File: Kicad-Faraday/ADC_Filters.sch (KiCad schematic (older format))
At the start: 14 parts

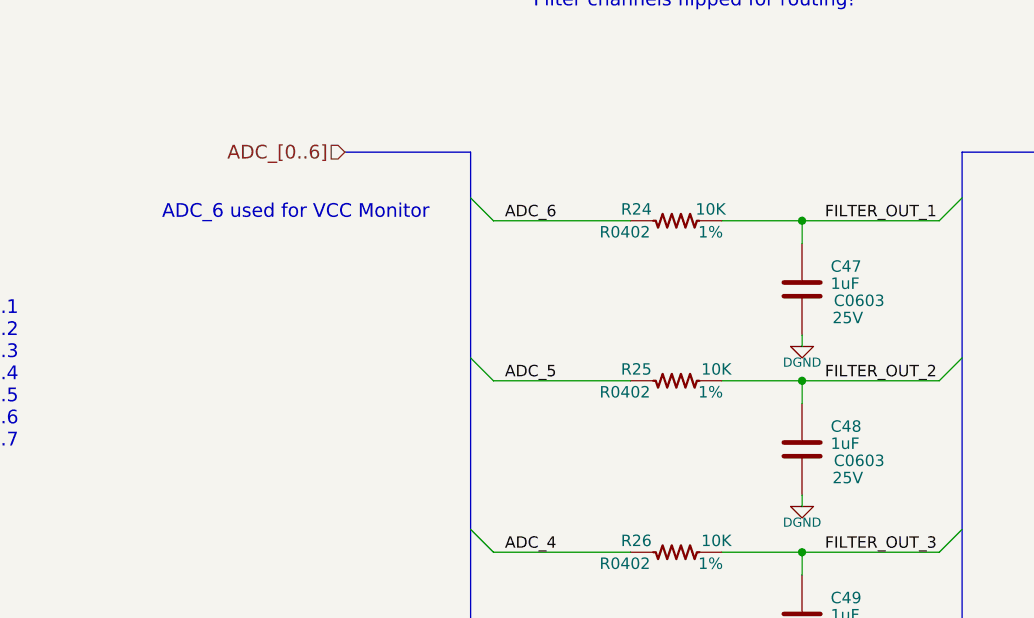
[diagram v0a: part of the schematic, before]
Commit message: Updated several items from the Rev B to C updates including microphone RC filter and CC1190 inductor footprints.
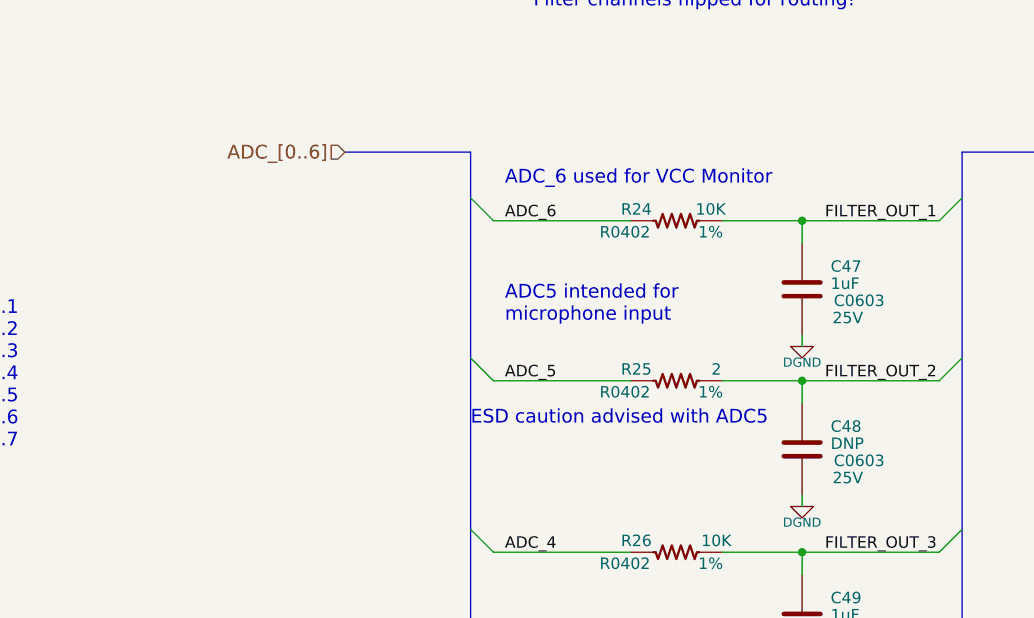
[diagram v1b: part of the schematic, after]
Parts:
- C48: value 1uF -> DNP
- R25: value 10K -> 2
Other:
- note added: "ADC5 intended for\nmicrophone input"
- note added: "ESD caution advised with ADC5"
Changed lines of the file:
@@
 Sheet 4 11
 Title "Faraday Wireless Node"
-Date "8 aug 2016"
+Date "18 oct 2016"
 Rev "C"
 Comp "FaradayRF"
@@
 P 8600 4350
 F 0 "R25" V 8650 4525 50  0000 C CNN
-F 1 "10K" V 8650 4175 50  0000 C CNN
+F 1 "2" V 8650 4175 50  0000 C CNN
 F 2 "R0402" V 8550 4575 50  0000 C CNN
 F 3 "" H 8600 4350 60  0000 C CNN
@@
 P 9150 4650
 F 0 "C48" H 9275 4750 50  0000 L CNN
-F 1 "1uF" H 9275 4675 50  0000 L CNN
+F 1 "DNP" H 9275 4675 50  0000 L CNN
 F 2 "C0603" H 9400 4600 50  0000 C CNN
 F 3 "" H 9150 4650 60  0000 C CNN
@@
 Text Notes 7975 2725 0    60   ~ 0
 Filter channels flipped for routing!
-Text Notes 6350 3650 0    60   ~ 0
+Text Notes 7850 3500 0    60   ~ 0
 ADC_6 used for VCC Monitor
 Text Notes 5150 4650 0    60   ~ 0
@@
 Wire Wire Line
 	9150 8600 9150 8650
+Text Notes 7850 4100 0    60   ~ 0
+ADC5 intended for\nmicrophone input
+Text Notes 7700 4550 0    60   ~ 0
+ESD caution advised with ADC5
 $EndSCHEMATC
